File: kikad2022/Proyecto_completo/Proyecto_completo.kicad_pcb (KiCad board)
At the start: 4 copper layers, 114.8 x 94.3 mm, 131 parts, among them IC2 LM393AD, IC3 74HC02PW,112, J1 Conn_01x02_Male, J10 Conn_01x01_Male, J11 Conn_01x01_Male, J16 Conn_01x01_Male, J17 Conn_01x02_Male, J18 Conn_01x01_Male, J19 Conn_01x01_Male, J2 Conn_01x01_Male, J20 V_Triang_RF, J21 Conn_01x01_Male, J4 Conn_01x01_Male, J5 Conn_01x01_Male, J6 Conn_01x01_Male, J7 Conn_01x01_Male, J9 Conn_01x01_Male, Q1 2N3906, Q10 2N3906, Q11 2N3904, Q12 2N7000, Q17 BC557, Q18 BC547, Q19 IRF510, Q2 2N3904, Q20 IRF510, Q21 BC557, Q22 Q_PMOS_DGS, Q3 2N3906, Q4 2N3904, Q5 2N3904, Q6 2N3904, Q7 2N7000, Q8 2N3906, Q9 2N3906, U1 OPA365xxDBV, U10 TL084, U2 TL082, U3 TL082, U5 LM393, U6 TLV3501AID, U8 IRS20957S, U9 TL084

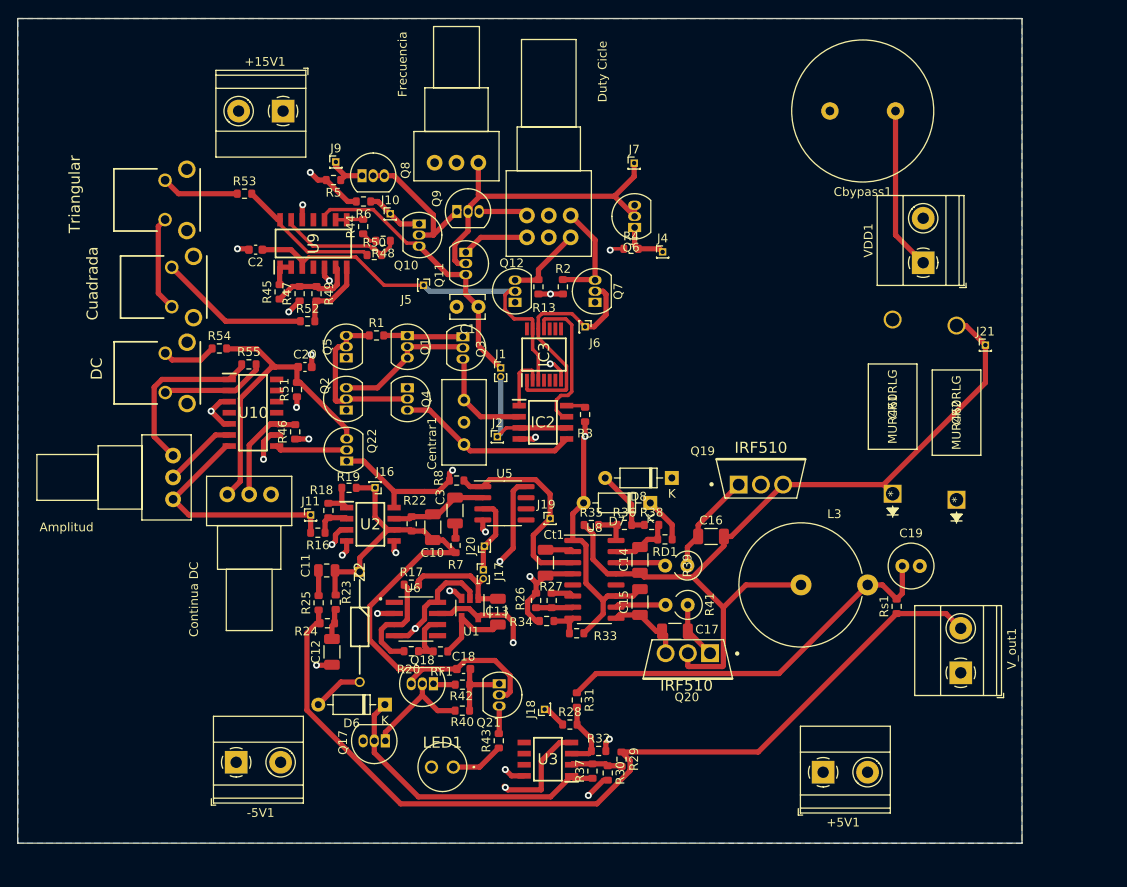
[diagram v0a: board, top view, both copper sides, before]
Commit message: kikad_modificaciones
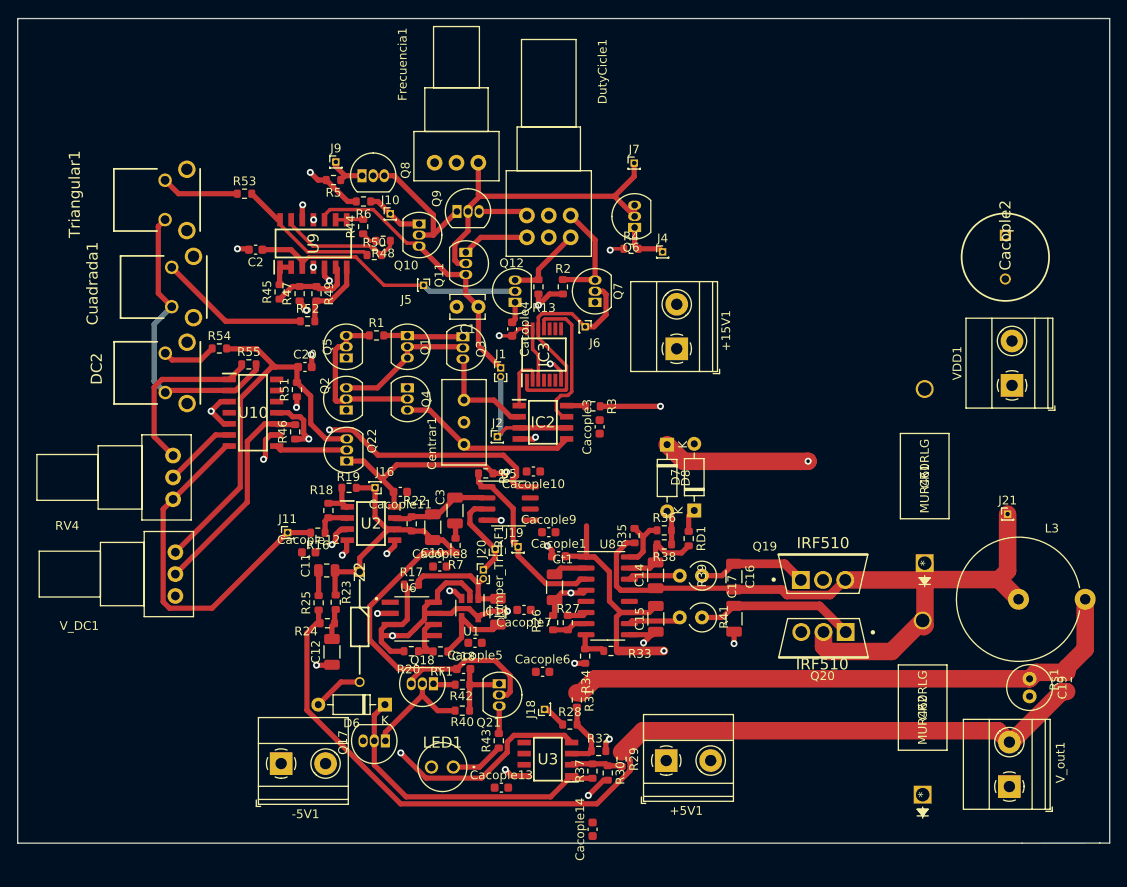
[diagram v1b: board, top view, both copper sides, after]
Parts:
- removed Cbypass1: 1000u, Capacitor_THT:C_Radial_D16.0mm_H25.0mm_P7.50mm
- removed J17: Conn_01x02_Male, Connector_PinHeader_1.00mm:PinHeader_1x02_P1.00mm_Vertical
- added Cacople1: 10p, Capacitor_SMD:C_0603_1608Metric, F.Cu at (207.4, 81.4)
- added Cacople10: 10p, Capacitor_SMD:C_0603_1608Metric, F.Cu at (204.5, 71.7)
- added Cacople11: 10p, Capacitor_SMD:C_0603_1608Metric, F.Cu at (189.3, 74.1)
- added Cacople12: 10p, Capacitor_SMD:C_0603_1608Metric, F.Cu at (178.8, 81.0)
- added Cacople13: 10p, Capacitor_SMD:C_0603_1608Metric, F.Cu at (200.8, 107.9)
- added Cacople14: 10p, Capacitor_SMD:C_0603_1608Metric, F.Cu at (211.2, 112.6)
- added Cacople2: 22n, New folder:CAPPRD500W65D1000H1350, F.Cu at (258.4, 44.7)
- added Cacople3: 10p, Capacitor_SMD:C_0603_1608Metric, F.Cu at (212.1, 66.6)
- added Cacople4: 10p, Capacitor_SMD:C_0603_1608Metric, F.Cu at (202.0, 55.5)
- added Cacople5: 10p, Capacitor_SMD:C_0603_1608Metric, F.Cu at (197.8, 91.3)
- added Cacople6: 10p, Capacitor_SMD:C_0603_1608Metric, F.Cu at (205.5, 94.6)
- added Cacople7: 10p, Capacitor_SMD:C_0603_1608Metric, F.Cu at (203.4, 87.6)
- added Cacople8: 10p, Capacitor_SMD:C_0603_1608Metric, F.Cu at (193.8, 82.6)
- added Cacople9: 10p, Capacitor_SMD:C_0603_1608Metric, F.Cu at (206.2, 78.7)
- added Jumper_Tri_RF1: Jumper_Tri_RF, Connector_PinHeader_1.00mm:PinHeader_1x02_P1.00mm_Vertical, F.Cu at (198.8, 83.0)
- DutyCicle1: renamed from Duty Cicle
- J16: value Conn_01x01_Male -> Realimentacion
- J19: value Conn_01x01_Male -> V_in_Driver
- J21: value Conn_01x01_Male -> L
- V_DC1: renamed from Continua DC
- moved +15V1 52.6 mm to (220.9, 57.7), turned to 90 degrees
- moved CR2 33.9 mm to (249.0, 108.7)
- moved L3 24.9 mm to (259.9, 86.3)
- moved Rs1 21.2 mm to (265.5, 95.5)
- moved J21 19.5 mm to (258.7, 76.6)
- moved C19 19.4 mm to (261.2, 95.4), turned to 270 degrees
- moved +5V1 18.0 mm to (219.7, 104.8)
- moved VDD1 17.3 mm to (259.2, 61.9)
- moved Q20 15.7 mm to (237.6, 90.8)
- moved V_out1 14.1 mm to (258.9, 107.8)
- moved Q19 13.0 mm to (237.6, 83.5)
- moved V_DC1 8.89 mm to (163.5, 81.0), turned to 180 degrees
- moved CR1 8.75 mm to (249.2, 82.2)
- moved C17 6.91 mm to (227.4, 88.6), turned to 270 degrees
- moved R34 5.95 mm to (210.4, 92.8), turned to 90 degrees
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- renumbered Cuadrada to Cuadrada1, DC to DC2, Frecuencia to Frecuencia1, Amplitud to RV4, Triangular to Triangular1
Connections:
- IC3 pad 14: Net-(IC3-Pad14) -> +5V
- U10 pad 11: (no net) -> -5V
- U10 pad 4: (no net) -> +15V
- U9 pad 11: Net-(U9-Pad11) -> -5V
- U9 pad 4: Net-(U9-Pad4) -> +15V
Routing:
- net +15V: track 48.2 -> 71.4 mm, vias 2 -> 4
- net Net-(C19-Pad1): track 46.4 -> 66.2 mm
- net /control2/Vo_control: track 27.4 -> 41.9 mm
- net Net-(R46-Pad2): track 11.9 -> 24.9 mm
- net Net-(C14-Pad1): track 97.1 -> 84.6 mm
- net Net-(C17-Pad1): track 6.60 -> 18.2 mm
- net Net-(C20-Pad1): track 37.0 -> 47.2 mm
- net +5V: track 35.8 -> 45.8 mm, vias 5 -> 6
- net -5V: track 76.1 -> 86.0 mm, vias 6 -> 7
- net /potencia/V_Out: track 103.9 -> 112.7 mm
- net /control/V_flipflop: track 46.3 -> 38.6 mm
- net Net-(D8-Pad2): track 8.09 -> 4.00 mm
- net Net-(R35-Pad2): track 3.97 -> 6.80 mm
- net Net-(C14-Pad2): track 7.05 -> 9.75 mm
- net Net-(J19-Pad1): track 23.8 -> 21.2 mm
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- added copper zone on In2.Cu, net +15V
- added copper zone on In2.Cu, net +5V
- added copper zone on In2.Cu, net -5V
- added copper zone on In1.Cu, net GND
- added copper zone on In2.Cu, net VD
- removed copper zone on In1.Cu, net +15V
- removed copper zone on In1.Cu, net +5V
- removed copper zone on In1.Cu, net -5V
- removed copper zone on B.Cu, net GND
- removed copper zone on In1.Cu, net VD
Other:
- board size 114.8 x 94.3 mm -> 124.9 x 94.3 mm
- net class Default: clearance 0.2 -> 0.3
- rule trace_clearance: 0.2 -> 0.3
- rule trace_min: 0.2 -> 0.3
